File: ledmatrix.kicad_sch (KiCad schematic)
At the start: 18 parts, among them J1 Conn_02x06_Odd_Even, J2 Conn_02x06_Odd_Even, J3 Conn_01x02, Q1 BSS84, Q2 BSS84, Q3 BSS84, Q4 BSS84, Q5 BSS84, Q6 BSS84, Q7 BSS84, Q8 BSS84, U1 mbi5029gd, U2 74HC137

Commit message: nicefy
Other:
- note added: "A: anodes (rows) G: mosfet "gates""
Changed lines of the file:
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@@
     (stroke (width 0) (type default) (color 0 0 0 0))
+  )
+  (text "A: anodes (rows)\nG: mosfet \"gates\"" (at 93.98 17.78 0)
+    (effects (font (size 1.27 1.27)) (justify left bottom))
   )
   (label "ROW_A0" (at 26.67 25.4 0)

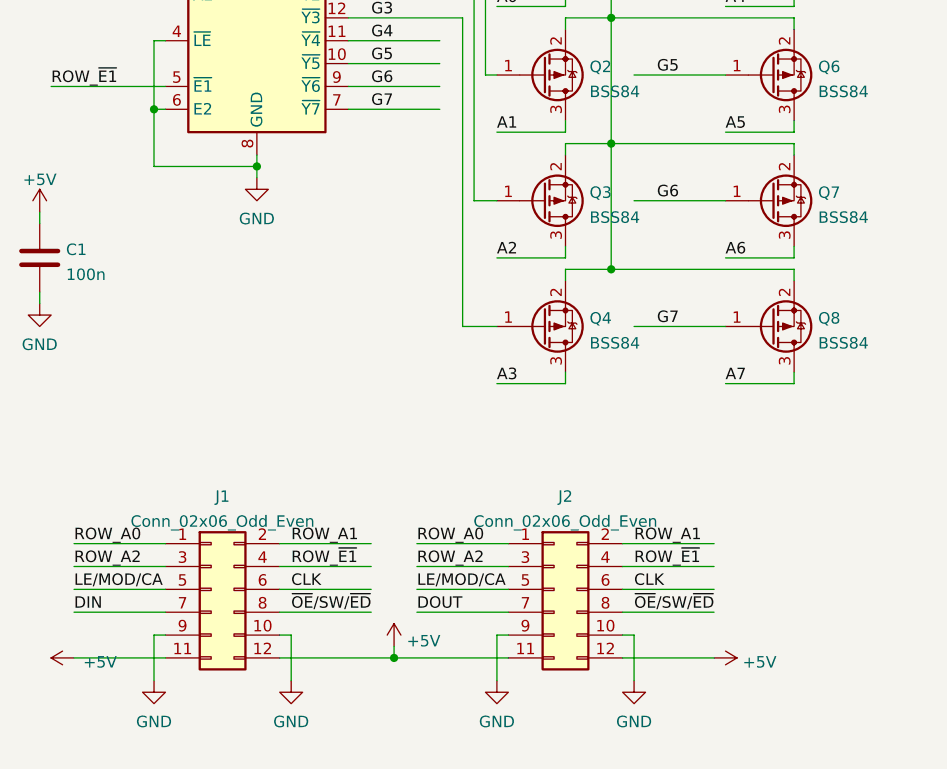
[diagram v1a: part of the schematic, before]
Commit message: changes, mostly adapting to proper JLCpcb 4layer rules
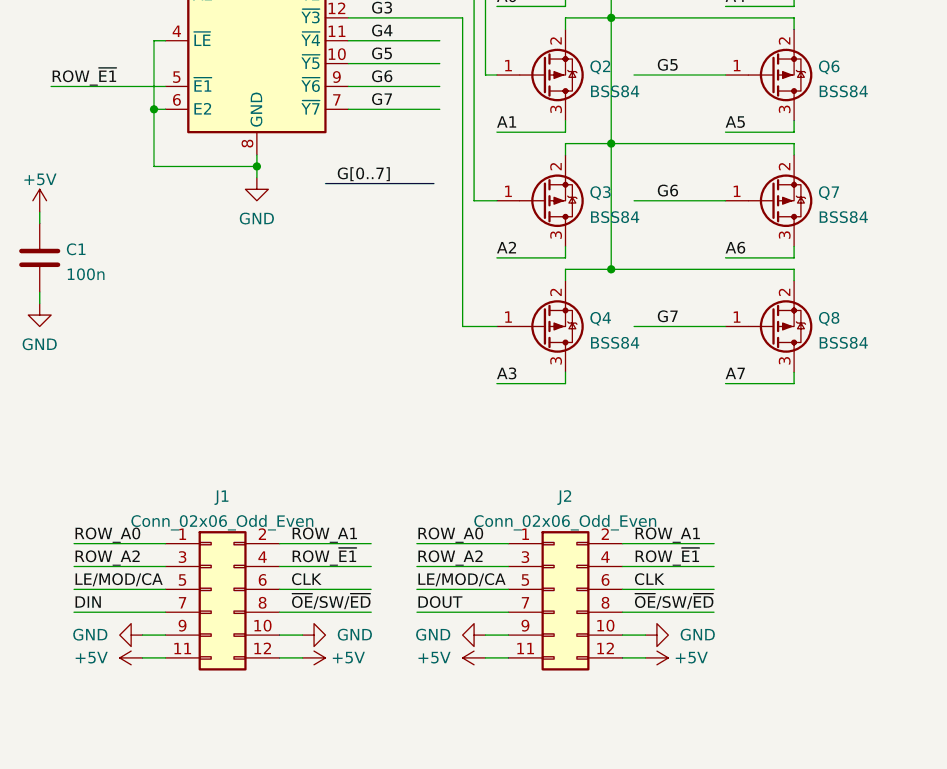
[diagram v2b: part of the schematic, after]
